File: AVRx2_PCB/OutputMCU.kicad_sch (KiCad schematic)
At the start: 25 parts, among them J1 DAC_OUT, J2 SPI, J3 RST, J4 DAC, J5 UPDI-0, J7 EXP, U1 AVR16EB28-I/SS, U10 MCP4726A0T-E/CH

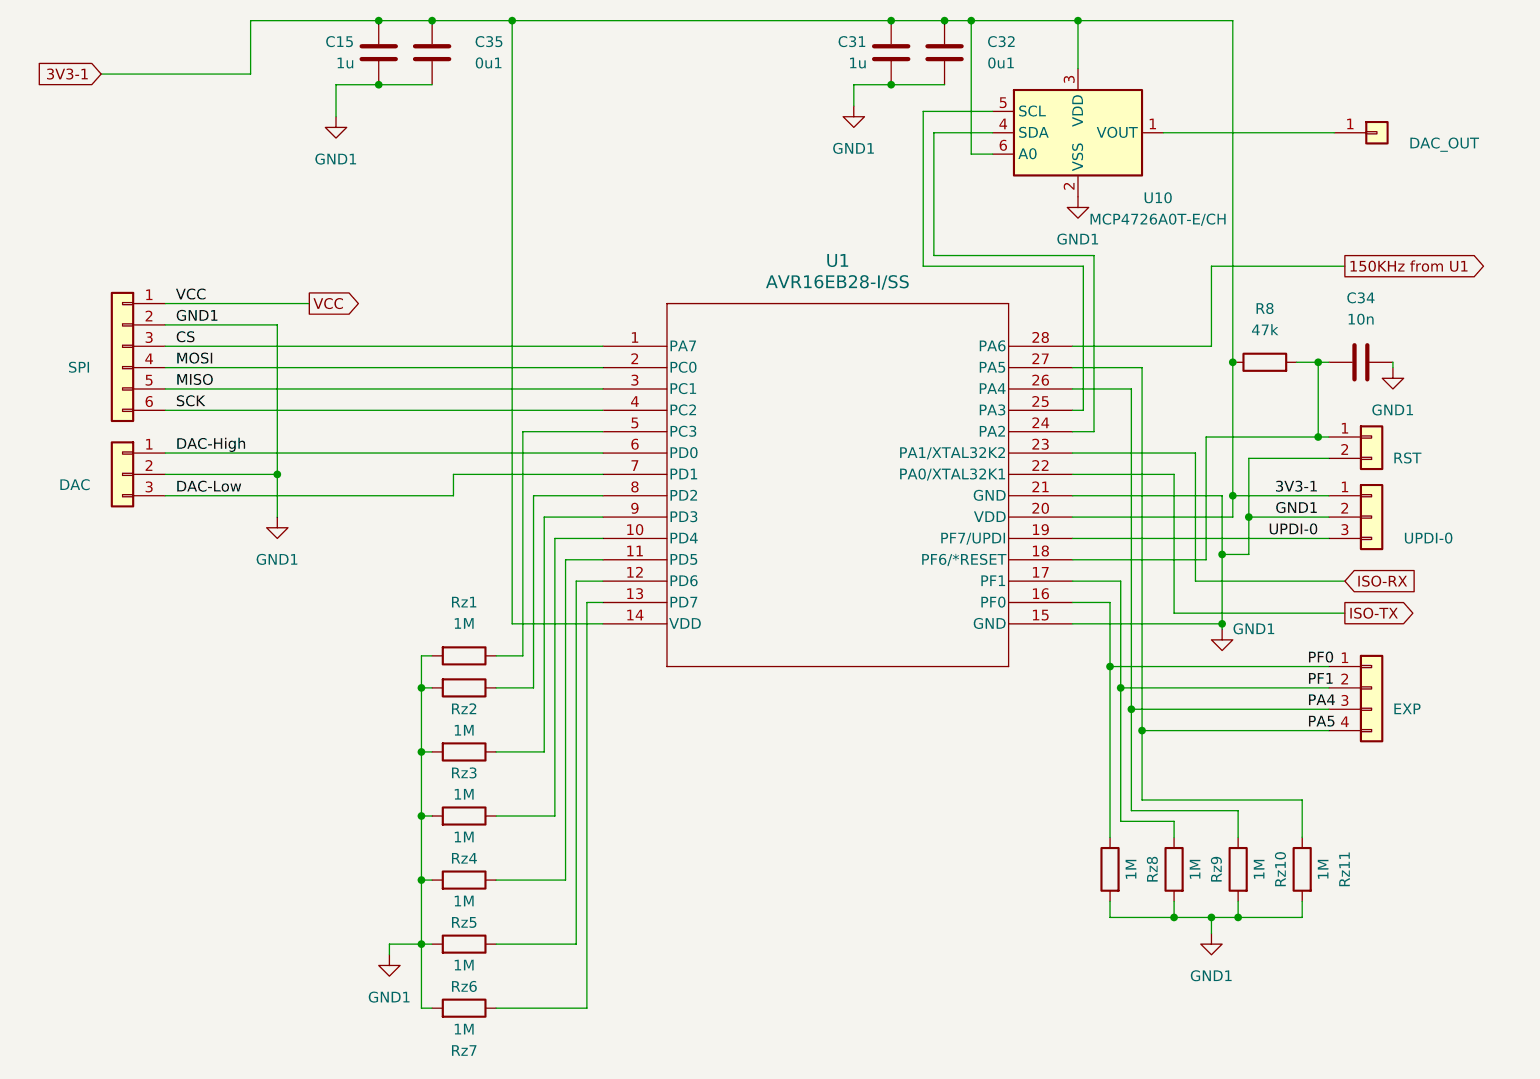
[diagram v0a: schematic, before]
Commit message: Fix a couple of switched traces
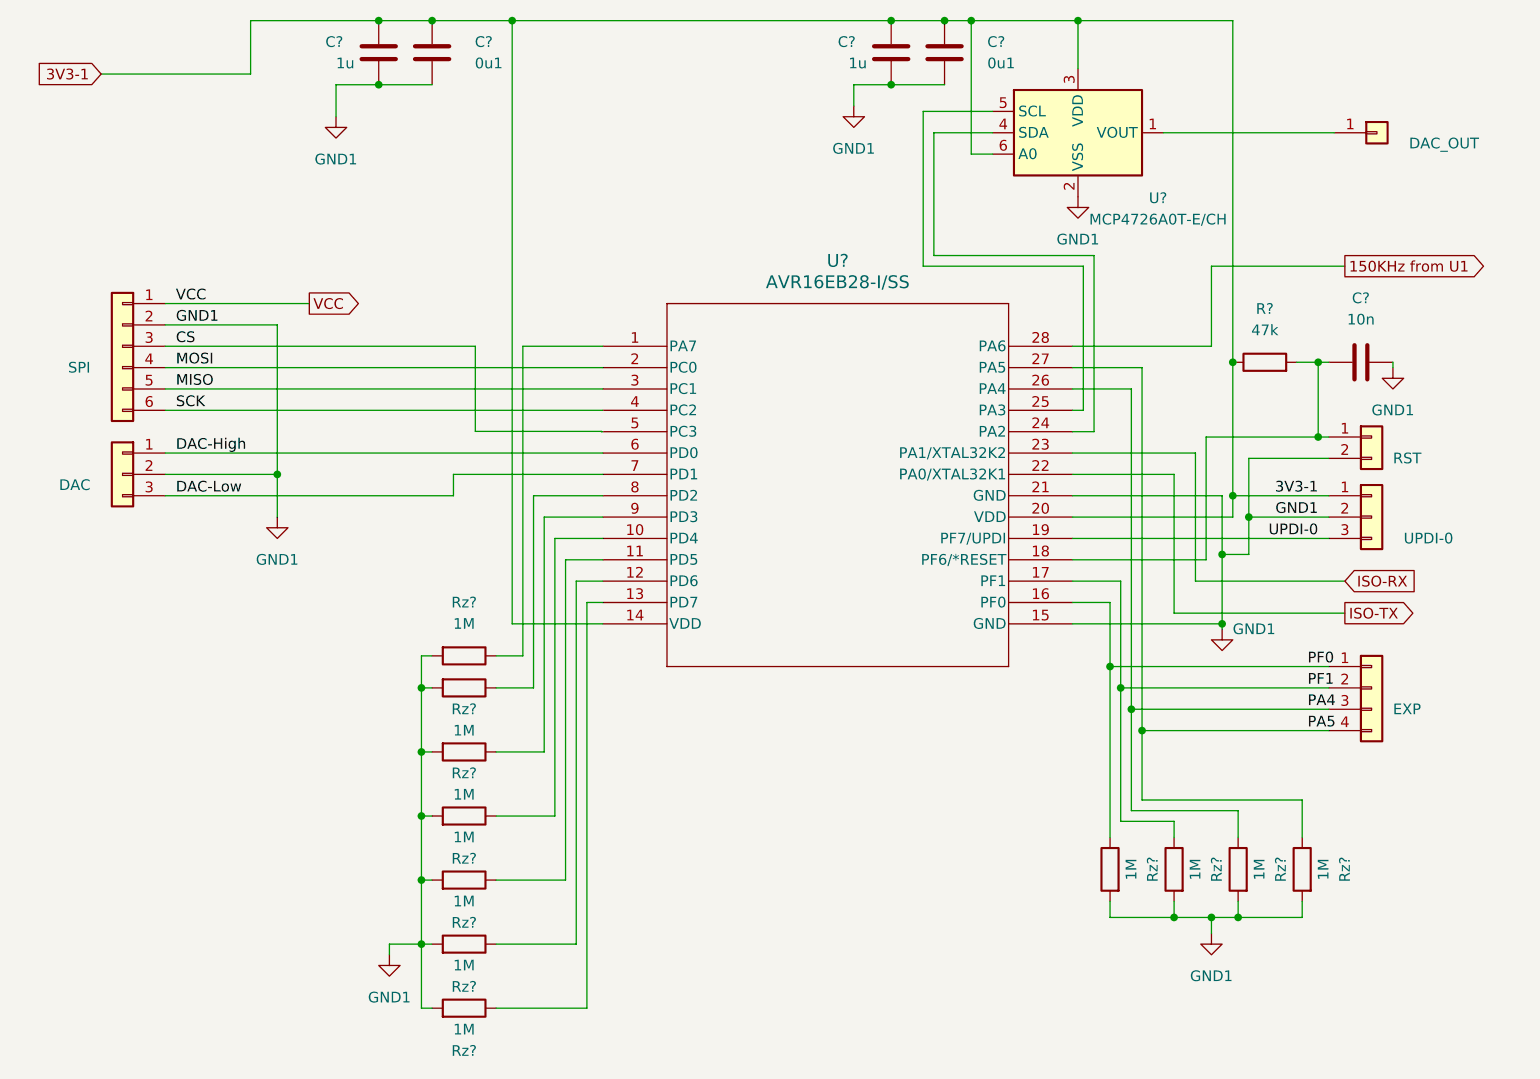
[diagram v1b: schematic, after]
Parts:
- renumbered C31 to C?, C35 to C?, C15 to C?, C34 to C?, C32 to C?, J7 to J?, J1 to J?, J4 to J?, J5 to J?, J3 to J?, J2 to J?, R8 to R?, Rz7 to Rz?, Rz9 to Rz?, Rz2 to Rz?, Rz1 to Rz?, Rz3 to Rz?, Rz5 to Rz?, Rz11 to Rz?, Rz8 to Rz?, Rz4 to Rz?, Rz10 to Rz?, Rz6 to Rz?, U10 to U?, U1 to U?
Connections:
- net CS: now also U?.5 (PC3); no longer U?.1 (PA7)
- net at Rz?.1: now also U?.1 (PA7); no longer U?.5 (PC3)

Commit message: Fix crossed traces that were found during prototype testing
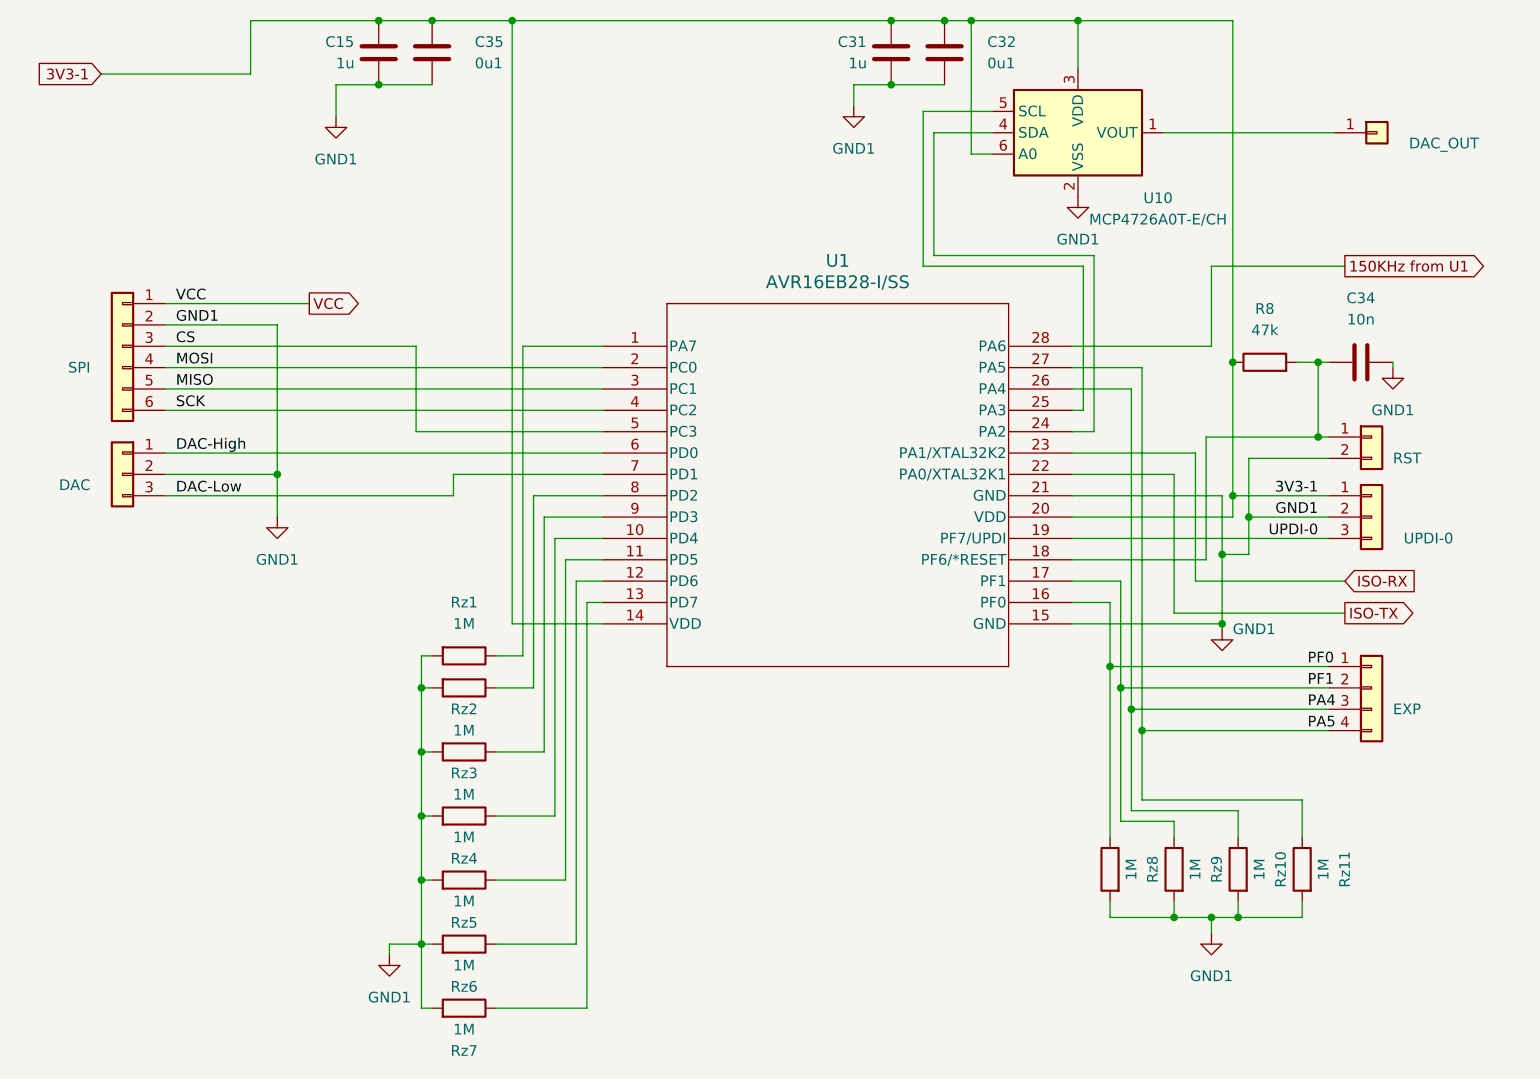
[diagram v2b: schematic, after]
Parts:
- gave numbers to parts that had none: 25
